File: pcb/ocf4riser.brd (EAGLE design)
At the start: 25.4 x 35.6 mm, 38 parts, among them IC1 STM32F405RGTx, IC2 MCP1703CB, IC3 W25Q80BV, IC4 TPD3E001DRL, IC5 STMPS2141STR, J1 TEENSY_3.1-3.2_DIL, J2 CORTEX_DEBUGNAKED, X1 TXC-7A

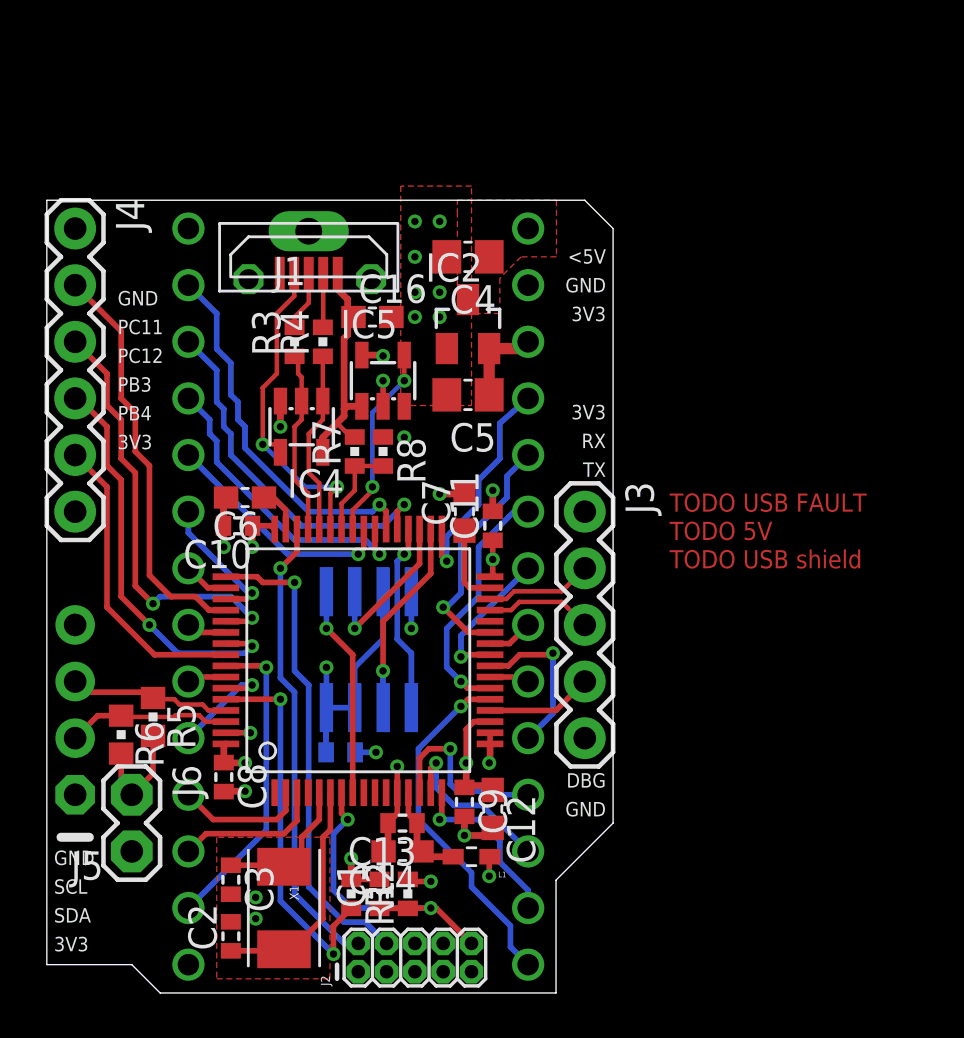
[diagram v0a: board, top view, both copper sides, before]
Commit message: Pin headers, values & names
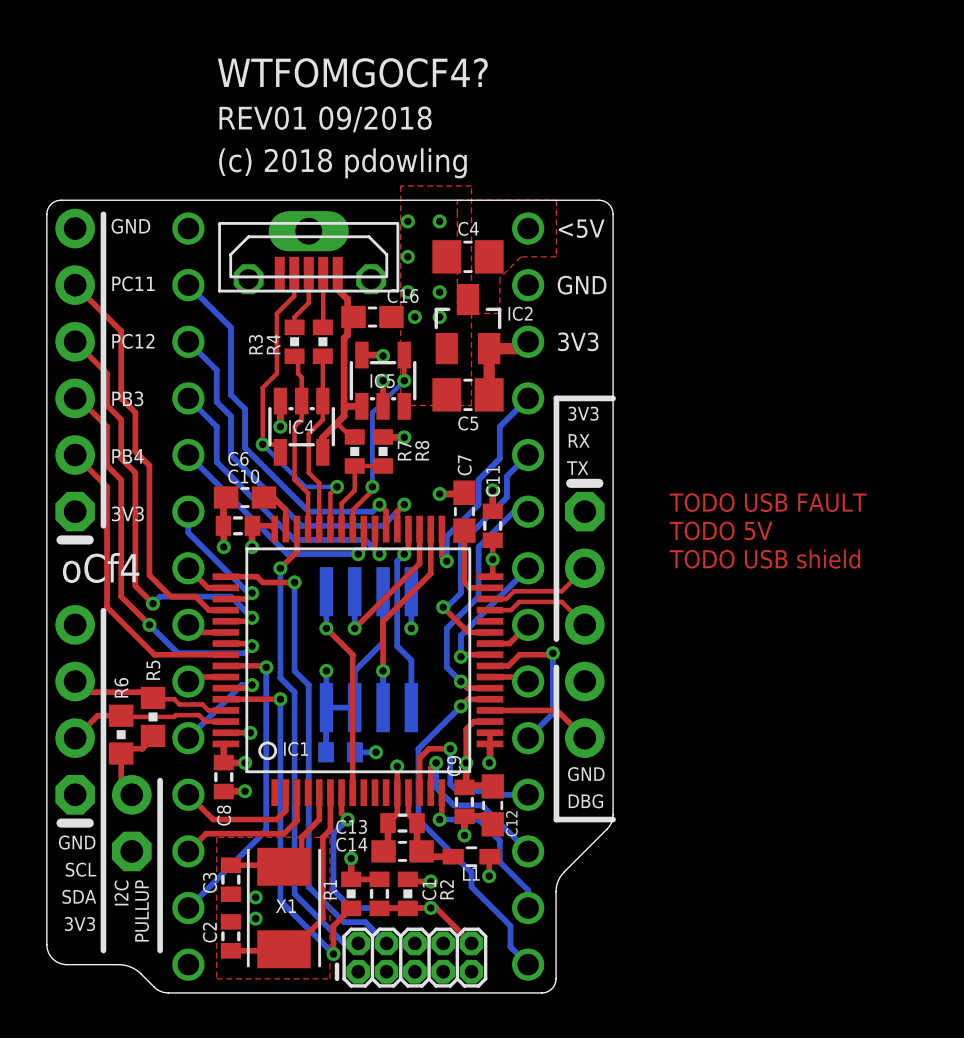
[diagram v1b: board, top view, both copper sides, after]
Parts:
- IC3: value W25Q80BV -> W25Q80BVSN; device pld-eeprom:SO08 -> pld-eeprom:SOIC-8
- J3: device SparkFun-Connectors:1X05 -> pld-headers:05X1-THIN
- J4: value (none) -> 06X1; device SparkFun-Connectors:1X06 -> pld-headers:06X1-THIN
- J5: device pld-misc:1X04_I2C_NOSILK -> pld-headers:04X1-THIN
- J6: value (none) -> 02X1; device SparkFun-Connectors:1X02 -> pld-headers:02X1-THIN
- moved J4 12.7 mm to (-3.81, 21.6), turned to 90 degrees
- moved J6 2.54 mm to (-1.27, 6.35), turned to 90 degrees
- moved C12 0.16 mm to (14.9, 8.41)
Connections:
- net +3V3: now also J4.1, J6.1; no longer J4.6, J6.2
- net DBG: now also J3.5; no longer J3.4
- net GND: now also J3.4, J4.6; no longer J3.5, J4.1
- net I2C_PU: now also J6.2; no longer J6.1
- net PB3: now also J4.3; no longer J4.4
- net PB4: now also J4.2; no longer J4.5
- net PC11: now also J4.5; no longer J4.2
- net PC12: now also J4.4; no longer J4.3
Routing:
- net I2C_PU: track 5.08 -> 3.86 mm
- net GND: track 21.2 -> 22.4 mm
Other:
- outline, holes or cut-outs redrawn
- board text added: "(c) 2018 pdowling"
- board text added: "3V3"
- board text added: "<5V"
- board text added: "GND"
- board text added: "GND DBG"
- board text added: "I2C PULLUP"
- board text added: "REV01 09/2018"
- board text added: "WTFOMGOCF4?"
- board text added: "oCf4"
- board text removed: "<5V GND 3V3"
- board text removed: "DBG GND"

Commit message: Tweaks
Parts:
- added C17: 22u, pld-rcl:C0805
- added L2: R/L, SparkFun-Passives:0805
- added R9: 47k, pld-rcl:R0402
- C16: value 4.7u -> 2.2u
- C2, C3: value (none) -> 33p
- J2: value CORTEX_DEBUGNAKED -> SWD/JTAG
- J3: value (none) -> DEBUG
- J4: value 06X1 -> IO
- J5: value (none) -> I2C
- USB: value MOLEX-105133 -> (none); device pld-usb-con:MOLEX-105133 -> pld-usb-con:614105150621
- moved C5 0.16 mm to (13.8, 27.0)
- moved USB 0.16 mm to (6.51, 33.0)
- moved C2 0.16 mm to (3.17, 2.38)
- moved X1 0.16 mm to (5.56, 3.65)
- moved C16 0.16 mm to (9.53, 30.2)
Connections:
- removed net !USB_FAULT: IC5.3
- new net !USB_PWR_FAULT: IC1.27, IC5.3, R9.1
- new net N$1: C17.1, J1.3.3V, L2.1
- net +3V3: now also L2.2, R9.2; no longer J1.3.3V
- net ENC_L1: now also IC1.28; no longer IC1.27
- net GND: now also C17.2, USB.Z1, USB.Z2; no longer USB.S1, USB.S2, USB.S3
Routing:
- net !USB_PWR_FAULT: track 0.00 -> 13.8 mm, vias 0 -> 2
- net N$1: track 0.00 -> 3.73 mm
- net GND: track 22.4 -> 24.1 mm, vias 23 -> 21
- net N$4: track 2.42 -> 4.02 mm
- net USB_ID: track 15.5 -> 17.0 mm
- net +3V3: track 27.3 -> 28.5 mm, vias 7 -> 10
- net N$7: track 2.67 -> 3.60 mm
- net ENC_L1: track 11.1 -> 10.2 mm
- net USB_VBUS: track 11.1 -> 11.7 mm
- net +5V: track 1.28 -> 1.07 mm, vias 1 -> 3
- added copper zone on layer 15, net +5V
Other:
- board text added: "3V3 RX< TX>"
- board text added: "I2C => PULLUP"
- board text added: "TODO USB port?"
- board text added: "We don't need no stinkin' Teensies!"
- board text added: "o_C+F4=?"
- board text removed: "3V3 RX TX"
- board text removed: "I2C PULLUP"
- board text removed: "TODO 5V"
- board text removed: "TODO USB FAULT"
- board text removed: "TODO USB shield"
- board text removed: "WTFOMGOCF4?"

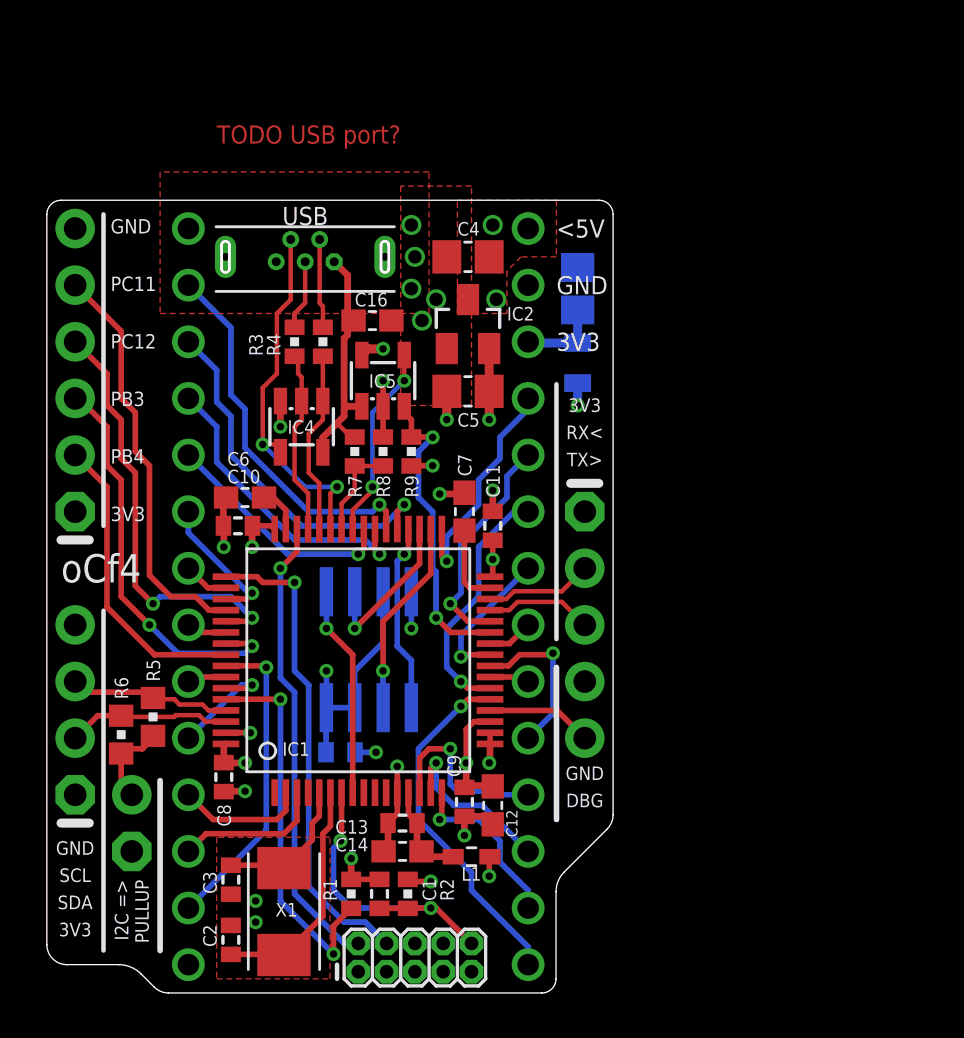
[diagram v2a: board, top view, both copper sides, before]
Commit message: USB as header instead of receptacle
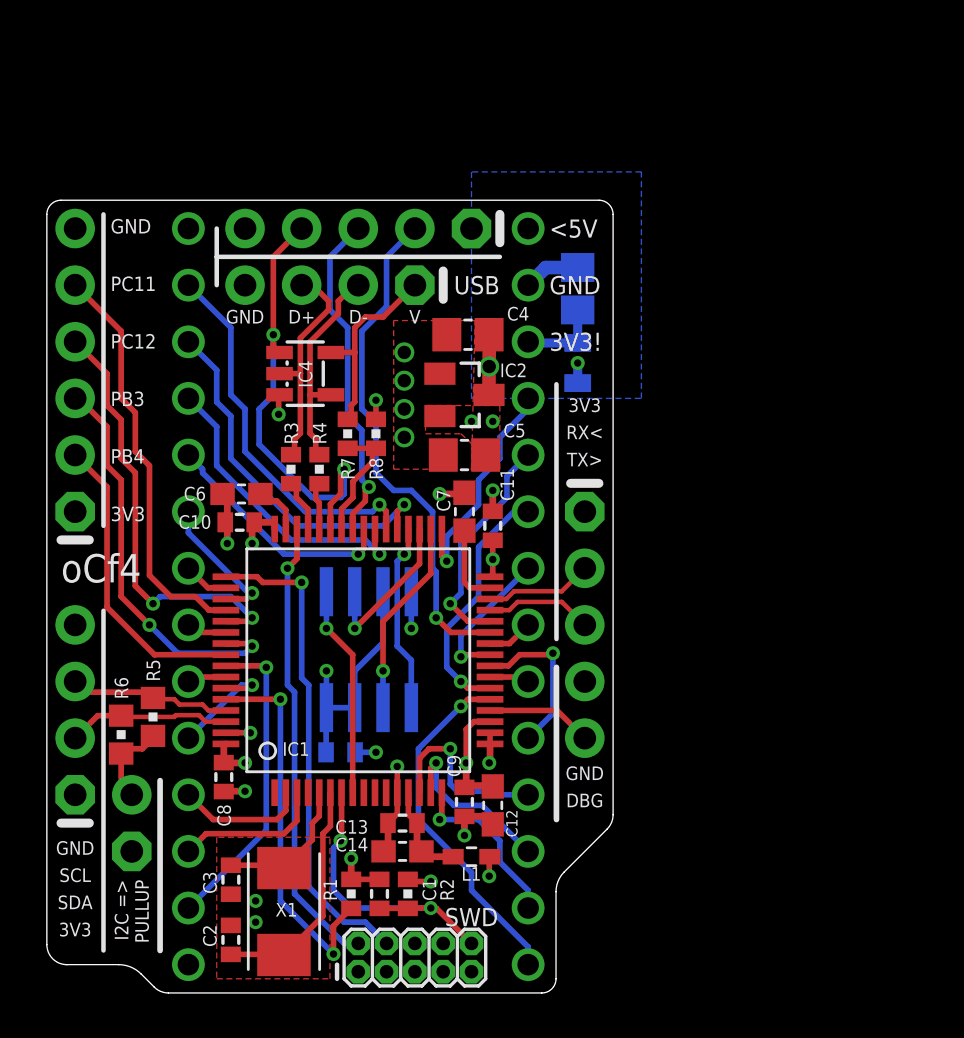
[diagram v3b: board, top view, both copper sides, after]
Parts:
- removed C16: 2.2u, pld-rcl:C0603
- removed IC5: STMPS2141STR, pld-usb-st:SOT23-5L
- removed R9: 47k, pld-rcl:R0402
- removed USB: (no value), pld-usb-con:614105150621
- added J7: USB, pld-headers:04X1-THIN
- added USBEX: USB, pld-headers:05X1-THIN
- moved R3 5.72 mm to (5.87, 23.5)
- moved R4 5.72 mm to (7.14, 23.5)
- moved C4 3.49 mm to (13.8, 29.5)
- moved IC2 3.18 mm to (13.7, 26.8), turned to 270 degrees
- moved C5 2.86 mm to (13.7, 24.1)
- moved IC4 2.39 mm to (6.51, 27.8), turned to 270 degrees
- moved R8 0.85 mm to (9.68, 25.1)
- moved R7 0.85 mm to (8.41, 25.1)
- moved C6 0.22 mm to (3.65, 22.4)
- moved C10 0.18 mm to (3.57, 21.1)
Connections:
- removed net N$4: R4.2, USB.2
- removed net N$7: R3.2, USB.3
- removed net USB_DM: IC1.44, IC4.1, R4.1
- removed net USB_DP: IC1.45, IC4.2, R3.1
- new net USB_I_N: IC4.4, J7.2, R4.2
- new net USB_I_P: IC4.2, J7.3, R3.2
- new net USB_N: IC1.44, R4.1
- new net USB_P: IC1.45, R3.1
- net !USB_PWR_EN: now also USBEX.3; no longer IC5.4
- net !USB_PWR_FAULT: now also USBEX.2; no longer IC5.3, R9.1
- net +3V3: now also USBEX.1; no longer R9.2
- net +5V: no longer IC5.5
- net GND: now also J7.4, USBEX.5; no longer C16.2, IC5.2, USB.5, USB.Z1, USB.Z2
- net USB_ID: now also IC4.1, USBEX.4; no longer IC4.4, USB.4
- net USB_VBUS: now also J7.1; no longer C16.1, IC5.1, USB.1
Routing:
- net USB_I_P: track 0.00 -> 10.0 mm
- net USB_I_N: track 0.00 -> 9.72 mm
- net !USB_PWR_FAULT: track 13.8 -> 23.0 mm, vias 2 -> 1
- net USB_DP: track 8.27 -> 0.00 mm
- net USB_DM: track 8.21 -> 0.00 mm
- net !USB_PWR_EN: track 8.77 -> 15.0 mm, vias 2 -> 1
- net +3V3: track 28.5 -> 24.4 mm
- net N$4: track 4.02 -> 0.00 mm
- net N$7: track 3.60 -> 0.00 mm
- net USB_ID: track 17.0 -> 20.3 mm
- net USB_VBUS: track 11.7 -> 8.81 mm
- net USB_P: track 0.00 -> 2.35 mm
- net USB_N: track 0.00 -> 2.17 mm
- net +5V: track 1.07 -> 2.70 mm, vias 3 -> 1
- net USB_VBUS_DET: track 4.35 -> 5.53 mm
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- added copper zone on layer 1, net +3V3
- added copper zone on layer 16, net +5V
- removed copper zone on layer 1, net +5V
- removed copper zone on layer 15, net +5V
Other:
- board text added: "3V3!"
- board text added: "D+"
- board text added: "D-"
- board text added: "SWD"
- board text added: "USB"
- board text added: "V"
- board text removed: "3V3"
- board text removed: "TODO USB port?"

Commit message: Tweaks
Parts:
- removed IC4: TPD3E001DRL, pld-usb-ti:SOT23-5L
- C2, C3: value 33p -> 27p
- L1: device EagleLibrary_Wuerth_Elektronik_eiSos_rev16a:WE-CBF_0603(W=2.6) -> EagleLibrary_Wuerth_Elektronik_eiSos_rev16a:WE-CBF_0603(W=2.2)
- moved R8 2.70 mm to (7.94, 27.1)
- moved R7 2.21 mm to (9.21, 27.1)
- moved L1 0.64 mm to (13.7, 5.56)
- moved C1 0.16 mm to (9.84, 4.29)
- moved R1 0.16 mm to (8.57, 4.29)
- moved R2 0.16 mm to (11.1, 4.29)
- moved C8 0.16 mm to (2.86, 9.53)
- moved C9 0.08 mm to (13.7, 8.49)
- moved C12 0.08 mm to (14.9, 8.49)
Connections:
- net GND: no longer IC4.3
- net USB_ID: no longer IC4.1
- net USB_I_N: no longer IC4.4
- net USB_I_P: no longer IC4.2
- net USB_VBUS: no longer IC4.5
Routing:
- net USB_VBUS: track 8.81 -> 4.87 mm
- net USB_ID: track 20.3 -> 17.2 mm
- net USB_VBUS_DET: track 5.53 -> 7.40 mm
- net GND: track 23.5 -> 22.2 mm, vias 19 -> 18
- net USB_I_P: track 10.0 -> 8.78 mm
- net !USB_PWR_FAULT: track 23.0 -> 22.0 mm
- net USB_I_N: track 9.72 -> 8.79 mm
- net ENC_R1: track 7.86 -> 7.35 mm
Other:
- board text added: "Buckle up back there"
- board text removed: "SWD"
